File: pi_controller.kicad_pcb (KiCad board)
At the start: 4 copper layers, 149 parts, among them J1 DC Supply, J10 CS5, J11 CS7, J12 ROW1, J13 ROW2, J14 ROW3, J15 LED1, J16 LED2, J17 LED3, J18 LED4, J19 ROW4, J2 I2C, J20 ROW5, J21 ROW6, J22 LED5, J23 LED6, J24 LED7, J25 LED8, J26 ROW7, J27 ROW8, J28 AN1, J29 AN3, J3 UART, J30 AN5, J31 AN7, J32 AN9, J33 AN11, J34 AN13, J35 AN15, J36 AN2, J37 AN4, J38 AN6, J39 AN8, J4 PWM, J40 AN10, J41 AN12, J42 AN14, J43 AN16, J5 CS2, J6 CS4, J7 CS6, J8 CS8, J9 CS3, Q1 AOD4184A, U1 AP62300TWU, U2 RaspberryPi_Pico, U3 LM4040DBZ-3, U4 74HC138, U5 74HC138, U6 TM1639 (TA2009B), U7 CD74HC4067SM96

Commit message: Update routing
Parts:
- added H1: MountingHole_Pad, MountingHole:MountingHole_2.2mm_M2_ISO14580_Pad_TopBottom, F.Cu at (196.0, 144.8)
- added H2: MountingHole_Pad, MountingHole:MountingHole_2.2mm_M2_ISO14580_Pad_TopBottom, F.Cu at (120.5, 61.2)
- added H3: MountingHole_Pad, MountingHole:MountingHole_2.2mm_M2_ISO14580_Pad_TopBottom, F.Cu at (196.1, 61.1)
- added H4: MountingHole_Pad, MountingHole:MountingHole_2.2mm_M2_ISO14580_Pad_TopBottom, F.Cu at (88.0, 145.0)
- moved J40 97.9 mm to (128.3, 70.9), turned to 180 degrees
- moved R2 96.5 mm to (149.9, 100.1)
- moved J41 96.5 mm to (136.1, 71.0), turned to 180 degrees
- moved R1 93.4 mm to (146.3, 100.1), turned to 180 degrees
- moved J2 93.4 mm to (151.5, 102.9), turned to -90 degrees
- moved J38 84.0 mm to (132.2, 78.9)
- moved J3 82.1 mm to (144.1, 110.2), turned to 90 degrees
- moved J37 80.7 mm to (140.1, 78.9)
- moved J32 77.7 mm to (124.3, 70.9), turned to 180 degrees
- moved J42 77.2 mm to (144.0, 71.0), turned to 180 degrees
- moved J30 76.9 mm to (136.1, 78.9)
- moved J33 76.8 mm to (132.2, 71.0), turned to 180 degrees
- moved J43 70.1 mm to (151.9, 70.9), turned to 180 degrees
- moved J39 69.5 mm to (124.3, 78.9)
- moved J34 68.4 mm to (140.1, 71.0), turned to 180 degrees
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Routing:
- net /COL_MUX_C: track 0.00 -> 169.2 mm, vias 0 -> 1
- net /COL_MUX_A: track 0.00 -> 167.8 mm, vias 0 -> 1
- net /COL_MUX_B: track 0.00 -> 153.4 mm, vias 0 -> 1
- net /MOSI: track 0.00 -> 125.6 mm, vias 0 -> 2
- net /SCLK: track 0.00 -> 113.8 mm, vias 0 -> 2
- net VDDA: track 6.54 -> 119.4 mm
- net /COL8: track 0.00 -> 107.0 mm
- net /COL1: track 0.00 -> 104.5 mm
- net /GRID1: track 0.00 -> 103.6 mm, vias 0 -> 1
- net /COL2: track 0.00 -> 103.2 mm
- net /COL3: track 0.00 -> 102.0 mm
- net /COL4: track 0.00 -> 101.5 mm
- net /COL5: track 0.00 -> 100.9 mm
- net /COL7: track 0.00 -> 100.5 mm
- net /COL6: track 0.00 -> 100.4 mm
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- added copper zone on In2.Cu, net +3V3
- added copper zone on In1.Cu, net GND
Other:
- board outline added: 114 x 88.8 mm

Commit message: Minor adjustments
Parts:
- moved J2 7.45 mm to (144.1, 101.7), turned to 90 degrees
- moved TP1 7.15 mm to (117.6, 105.8)
- moved TP4 6.22 mm to (110.9, 105.7)
- moved R2 6.07 mm to (145.8, 104.5), turned to 180 degrees
- moved R1 5.38 mm to (149.3, 104.5), turned to 0 degrees
- moved C7 0.13 mm to (102.6, 93.0)
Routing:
- net /SDA: track 2.80 -> 54.1 mm, vias 0 -> 1
- net /SCL: track 3.12 -> 53.7 mm, vias 0 -> 1
- net /SCLK: track 113.8 -> 121.3 mm
- net VDDA: track 119.4 -> 113.2 mm
- net /CS_KEY: track 79.3 -> 84.5 mm
- net /UART0_RX: track 21.3 -> 25.3 mm
- net /COL_MUX_B: track 153.4 -> 156.9 mm
- net +9V: track 0.00 -> 2.72 mm
- net GND: track 64.2 -> 66.6 mm, vias 22 -> 24
- net /PWM_OUT: track 22.8 -> 23.6 mm
- net /AN14: track 39.4 -> 38.8 mm
- net /AN16: track 43.4 -> 44.0 mm
- net /ADC_MUX_D: vias 1 -> 3

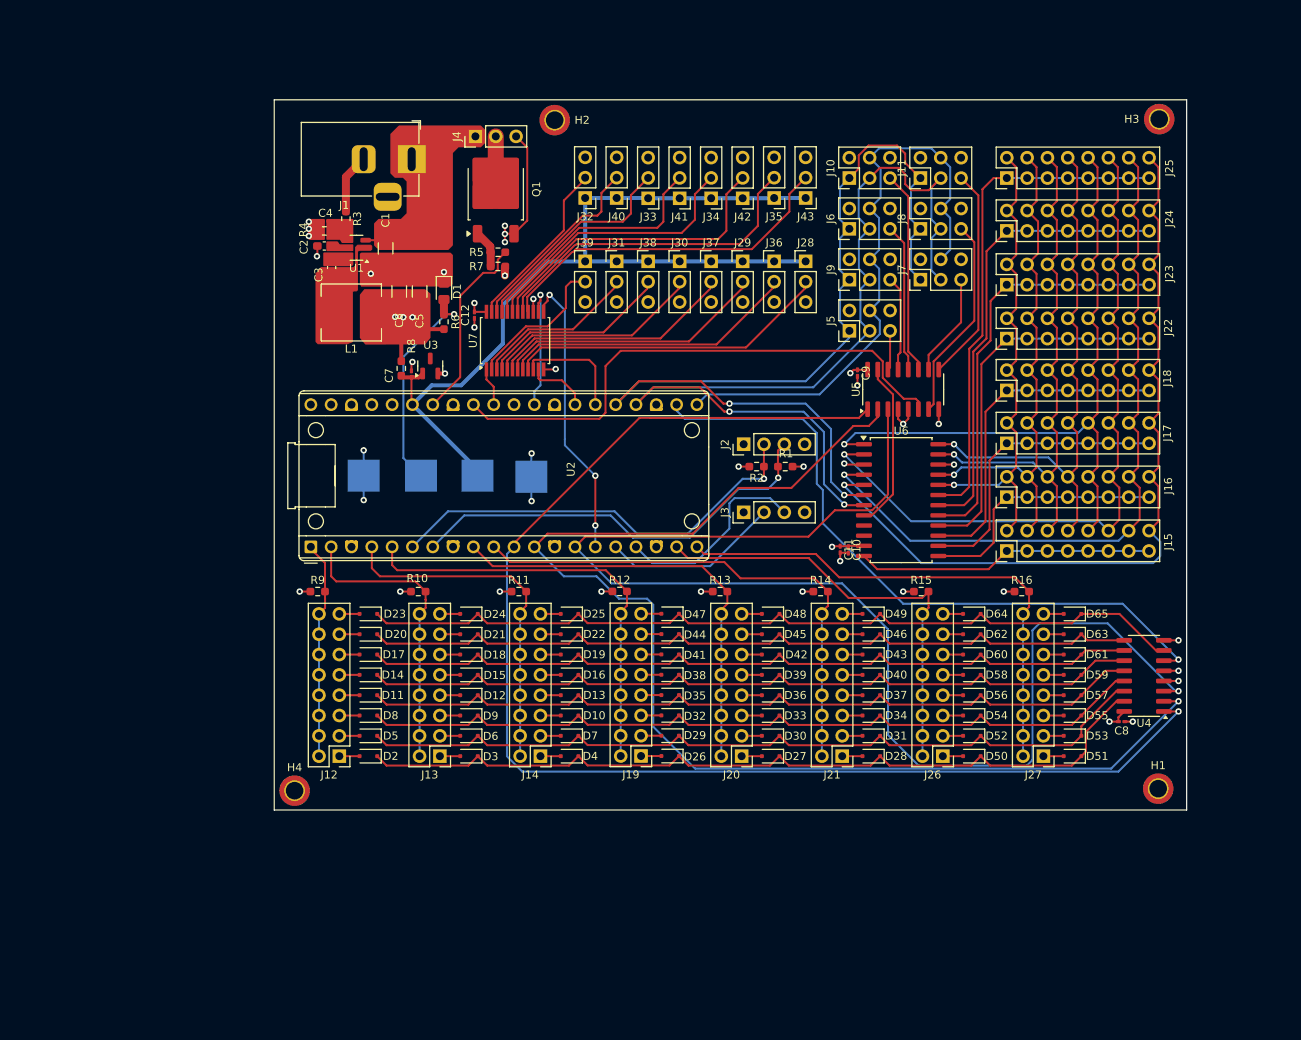
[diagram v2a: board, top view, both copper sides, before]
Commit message: Component repositioning to compact form factor
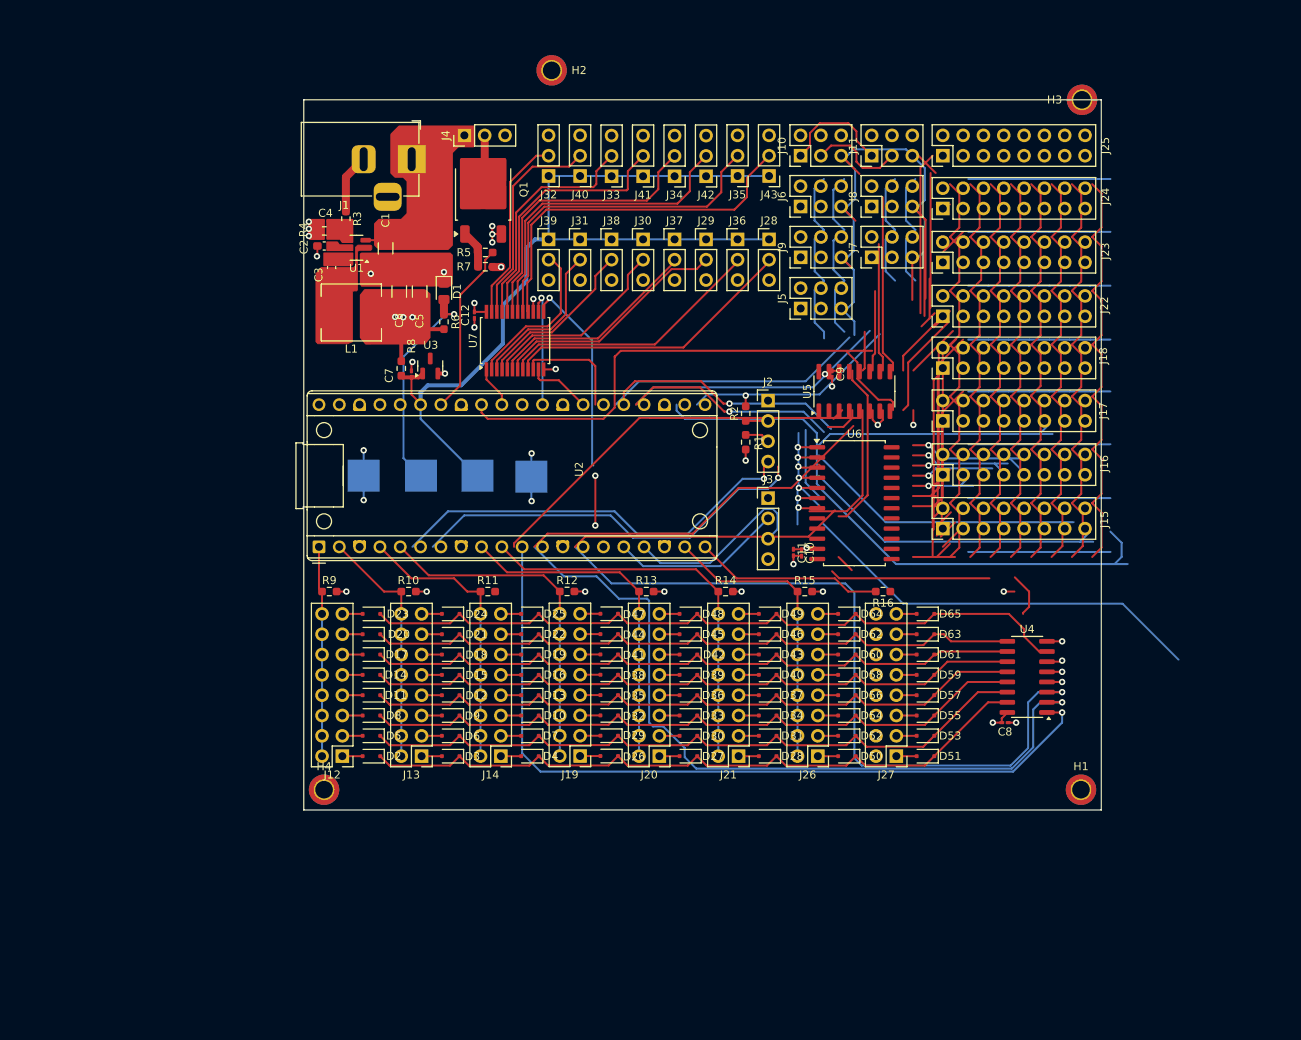
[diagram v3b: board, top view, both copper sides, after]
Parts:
- moved D51 18.4 mm to (166.9, 140.7)
- moved D53 18.4 mm to (166.9, 138.2)
- moved D55 18.4 mm to (166.9, 135.6)
- moved D57 18.4 mm to (166.9, 133.1)
- moved D59 18.4 mm to (166.9, 130.6)
- moved D61 18.4 mm to (166.9, 128.0)
- moved D63 18.4 mm to (166.9, 125.5)
- moved D65 18.4 mm to (166.9, 122.9)
- moved J27 18.4 mm to (163.2, 140.7)
- moved R16 17.3 mm to (161.6, 120.1), turned to 180 degrees
- moved D50 15.6 mm to (157.1, 140.7)
- moved D52 15.6 mm to (157.1, 138.2)
- moved D54 15.6 mm to (157.1, 135.6)
- moved D56 15.6 mm to (157.1, 133.1)
- moved D58 15.6 mm to (157.1, 130.6)
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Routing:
- net /ROW8: track 64.7 -> 23.7 mm
- net /COL_MUX_C: track 169.2 -> 145.8 mm
- net /SEG12: track 63.6 -> 41.3 mm
- net /CS1: track 21.1 -> 0.00 mm
- net /SEG9: track 46.8 -> 67.1 mm
- net /ROW7: track 55.4 -> 37.0 mm
- net GND: track 66.6 -> 84.7 mm, vias 24 -> 26
- net /GRID5: track 71.3 -> 53.4 mm, vias 1 -> 0
- net /COL1: track 104.5 -> 88.0 mm
- net /COL_MUX_A: track 167.8 -> 151.5 mm
- net /CS8: track 25.6 -> 41.4 mm
- net /COL2: track 103.2 -> 87.6 mm
- net /COL4: track 101.5 -> 86.4 mm
- net /COL5: track 100.9 -> 85.9 mm
- net /COL3: track 102.0 -> 86.9 mm
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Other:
- board size 114 x 88.8 mm -> 99.7 x 88.8 mm

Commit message: Adjusting DRC checks
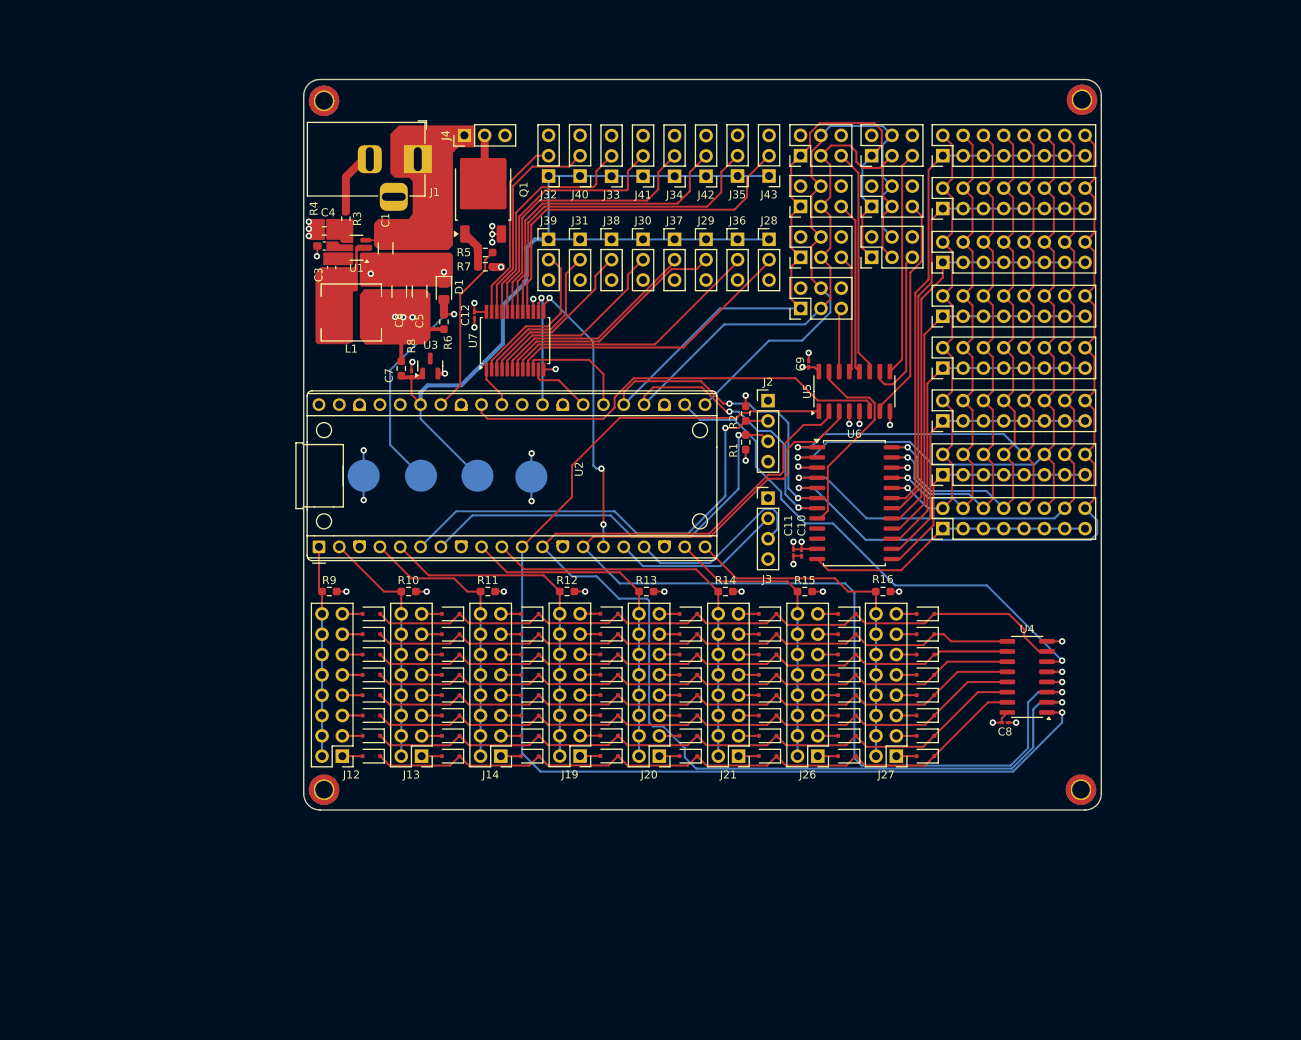
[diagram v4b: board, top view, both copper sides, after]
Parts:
- TP1, TP2, TP3, TP4: footprint TestPoint:TestPoint_Pad_4.0x4.0mm -> TestPoint:TestPoint_Pad_D4.0mm
- moved H2 28.7 mm to (91.7, 58.8)
- moved C9 3.18 mm to (152.3, 91.7), turned to 90 degrees
- moved J1 0.76 mm to (103.4, 66.1)
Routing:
- net GND: track 84.7 -> 51.2 mm, vias 26 -> 25
- net /CS1: track 0.00 -> 25.5 mm
- net /SEG12: track 41.3 -> 64.2 mm
- net /MISO: track 91.3 -> 70.5 mm
- net /ROW8: track 23.7 -> 44.2 mm
- net /SEG9: track 67.1 -> 47.6 mm
- net /GRID5: track 53.4 -> 72.2 mm, vias 0 -> 1
- net /CS_KEY: track 80.3 -> 64.7 mm
- net /CS5: track 13.3 -> 28.5 mm
- net /CS6: track 5.33 -> 19.8 mm
- net /SEG3: track 50.2 -> 37.0 mm, vias 1 -> 0
- net /CS8: track 41.4 -> 28.2 mm
- net /CS3: track 1.84 -> 14.9 mm
- net /CS_LED: track 68.0 -> 55.0 mm
- net /SCLK: track 121.3 -> 108.7 mm
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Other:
- board size 99.7 x 88.8 mm -> 99.7 x 91.3 mm
- board text added: "2.03 x 2.03 radius"

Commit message: Update PCB footprints
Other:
- board text added: "Analog Inputs 1- VDA 2- Wiper 3- Gnd"
- board text added: "SPI Interfaces"
- board text added: "UART"
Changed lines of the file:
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@@
 		(tags "resistor handsolder")
 		(property "Reference" "R1"
-			(at 1.016 1.524 90)
+			(at 0.635 1.397 90)
 			(layer "F.SilkS")
 			(effects
@@
 		)
 		(fp_line
-			(start 0.9 1.9)
+			(start 0.9 2)
 			(end 0.9 4.6)
 			(stroke
@@
 		(tags "resistor handsolder")
 		(property "Reference" "R2"
-			(at -1.0395 -1.524 90)
+			(at -1.0395 -1.397 90)
 			(layer "F.SilkS")
 			(effects
@@
 		(attr through_hole)
 		(fp_line
-			(start 4.11 -27.01)
-			(end 4.11 -26.09)
+			(start 10 -25.61)
+			(end 7.51 -25.61)
 			(stroke
 				(width 0.12)
@@
 		)
 		(fp_line
-			(start -4.11 -27.01)
-			(end 4.11 -27.01)
+			(start 7.51 -25.61)
+			(end 7.51 -24.69648)
 			(stroke
 				(width 0.12)
@@
 		)
 		(fp_line
-			(start -4.11 -27.01)
-			(end -4.11 -26.09)
+			(start 4.17 -25.61)
+			(end 7.51 -25.61)
 			(stroke
 				(width 0.12)
@@
 		)
 		(fp_line
-			(start 4.11 -26.09)
-			(end 3.9 -26.09)
+			(start -3.97 -25.61)
+			(end 4.28 -25.61)
 			(stroke
 				(width 0.12)
@@
 		)
 		(fp_line
-			(start 3.9 -26.09)
-			(end 3.9 -24.694)
+			(start -7.51 -25.61)
+			(end -3.97 -25.61)
 			(stroke
 				(width 0.12)
@@
 		)
 		(fp_line
-			(start -3.9 -26.09)
-			(end -3.9 -24.694)
+			(start -7.51 -25.61)
+			(end -7.51 -24.69648)
 			(stroke
 				(width 0.12)
@@
 		)
 		(fp_line
-			(start -4.11 -26.09)
-			(end -3.9 -26.09)
+			(start -10 -25.61)
+			(end -7.51 -25.61)
 			(stroke
 				(width 0.12)
@@
 		)
 		(fp_line
-			(start 10 -25.61)
-			(end 7.51 -25.61)
+			(start 4.11 -25.6032)
+			(end 4.11 -24.6832)
 			(stroke
 				(width 0.12)
@@
 		)
 		(fp_line
-			(start 7.51 -25.61)
-			(end 7.51 -24.69648)
+			(start -4.11 -25.6032)
+			(end -4.11 -24.6832)
 			(stroke
 				(width 0.12)
@@
 		)
 		(fp_line
-			(start 4.235 -25.61)
-			(end 7.51 -25.61)
+			(start -10.27 -25.547)
+			(end -10.27 25.547)
 			(stroke
 				(width 0.12)
@@
 		)
 		(fp_line
-			(start -4.235 -25.61)
-			(end 4.235 -25.61)
+			(start 10.61 -25)
+			(end 10.61 25)
 			(stroke
 				(width 0.12)
@@
 		)
 		(fp_line
-			(start -7.51 -25.61)
-			(end -4.235 -25.61)
+			(start -10.61 -25)
+			(end -10.61 25)
 			(stroke
 				(width 0.12)
@@
 		)
 		(fp_line
-			(start -7.51 -25.61)
-			(end -7.51 -24.69648)
+			(start 7.51 -24.69648)
+			(end 7.51 -22.30352)
 			(stroke
 				(width 0.12)
@@
 		)
 		(fp_line
-			(start -10 -25.61)
-			(end -7.51 -25.61)
+			(start -7.51 -24.69648)
+			(end -7.51 -22.30352)
 			(stroke
 				(width 0.12)
@@
 		)
 		(fp_line
-			(start -10.27 -25.547)
-			(end -10.27 25.547)
+			(start 3.9 -24.694)
+			(end 3.9 -22.306)
 			(stroke
 				(width 0.12)
-				(type solid)
+				(type default)
 			)
 			(layer "F.SilkS")
 		)
 		(fp_line
-			(start 10.61 -25)
-			(end 10.61 25)
+			(start -3.9 -24.694)
+			(end -3.9 -22.306)
 			(stroke
 				(width 0.12)
-				(type solid)
+				(type default)
 			)
 			(layer "F.SilkS")
 		)
 		(fp_line
-			(start -10.61 -25)
-			(end -10.61 25)
+			(start 4.11 -24.6832)
+			(end 3.9 -24.6832)
 			(stroke
 				(width 0.12)
@@
 		)
 		(fp_line
-			(start 7.51 -24.69648)
-			(end 7.51 -22.30352)
+			(start 3.9 -24.6832)
+			(end 3.9 -23.2872)
 			(stroke
 				(width 0.12)
@@
 		)
 		(fp_line
-			(start -7.51 -24.69648)
-			(end -7.51 -22.30352)
+			(start -3.9 -24.6832)
+			(end -3.9 -23.2872)
 			(stroke
 				(width 0.12)
@@
 		)
 		(fp_line
-			(start 3.9 -24.694)
-			(end 3.9 -22.306)
+			(start -4.11 -24.6832)
+			(end -3.9 -24.6832)
 			(stroke
 				(width 0.12)
-				(type default)
-			)
-			(layer "F.SilkS")
-		)
-		(fp_line
-			(start -3.9 -24.694)
-			(end -3.9 -22.306)
-			(stroke
-				(width 0.12)
-				(type default)
+				(type solid)
 			)
 			(layer "F.SilkS")
@@
 		(fp_poly
 			(pts
-				(xy 3.79 -21.2) (xy 3.79 -26.2) (xy 4 -26.2) (xy 4 -26.9) (xy -4 -26.9) (xy -4 -26.2) (xy -3.79 -26.2)
-				(xy -3.79 -21.2)
+				(xy 3.79 -21.2) (xy 3.79 -24.7904) (xy 4.0132 -24.7904) (xy 4.0132 -25.3492) (xy -4.0132 -25.3492)
+				(xy -4.0132 -24.7904) (xy -3.79 -24.7904) (xy -3.79 -21.2)
 			)
 			(stroke
@@
 		)
 		(fp_text user "${REFERENCE}"
-			(at 0 0 360)
+			(at 0.084 24.401 -90)
 			(layer "F.Fab")
 			(effects
@@
 		)
 		(group ""
-			(members "2646626f-3226-476e-bf4c-3d579709c044" "3704ffaa-dbbb-4da7-858c-14cb0424dd8d"
-				"4ba47d3a-43f8-4097-bc15-458fb810d474" "687c525b-7fe1-4e01-9ef9-63893dd76d1e"
-				"738a19d3-20ee-454a-ada1-3f4b2cac0b83" "93851b35-f911-4533-b25b-d64fbfd2a055"
-				"b19894cc-233f-4fca-b0ad-4d6b157d2181" "e088057c-4a2a-4883-b166-cee210829a6f"
-			)
-		)
-		(group ""
-			(members "5be00809-793c-4575-88c9-af6c156cc3e3" "5dc808f1-1ad2-4d82-b53a-339be024c766"
-				"61b49ba1-e006-429b-9a0e-e9dea97ee073" "646aa24a-b73b-41c0-a789-7f6e55234bf8"
-				"7884036b-77c5-4ebb-b68a-e1c50022c9ea" "849cfad4-072e-4d0f-a78f-95159eca27bb"
-				"8f0c9811-345c-4f6f-80b3-119b2904208e" "9b58e8fa-1eed-499b-aafd-84898567d050"
-				"c4036112-574f-486a-a8de-72c6bea74aa9" "dfe2bc5d-9716-4555-8132-bbd50e759a71"
-				"e701a5ba-01e5-430d-a5b0-014c02f8d0aa" "eff28fdf-8093-467d-81fe-f5fe5485abcd"
-			)
-		)
-		(group ""
 			(members "6207e867-1a35-47a8-8ce9-ad636b722732" "65c75b9c-4f2d-401d-853f-fac93e4d7d40")
 		)
@@
 				"4c075adb-7bfb-4d79-b53a-99b1b90aa57b" "563b85e2-65d0-46b2-b2c9-adc0f08d7a8c"
 				"81f87357-9f09-4fd2-8eca-16dfedbfb7df" "8af63139-80e0-4d1f-835c-ff931e5a9630"
-				"c5128fa3-bcb7-4315-bd03-ec95c603f6d8" "c7623e52-15f2-4cd6-acee-7c920f71d378"
-				"d2afa5d6-e4b2-47e9-abf4-1ff90d90d2ff" "d7d20f5e-8ea0-4fb9-a0c3-7fedcb7f0ddb"
-				"d82fe402-44ed-48ec-ae53-c13e327d779e"
+				"c5128fa3-bcb7-4315-bd03-ec95c603f6d8" "d2afa5d6-e4b2-47e9-abf4-1ff90d90d2ff"
+				"d7d20f5e-8ea0-4fb9-a0c3-7fedcb7f0ddb" "d82fe402-44ed-48ec-ae53-c13e327d779e"
 			)
 		)
@@
 		(layer "Edge.Cuts")
 	)
+	(gr_text "SPI Interfaces"
+		(at 149.86 88.392 0)
+		(layer "F.SilkS")
+		(effects
+			(font
+				(size 1 1)
+				(thickness 0.15)
+			)
+			(justify left bottom)
+		)
+	)
+	(gr_text "UART"
+		(at 145.288 115.316 90)
+		(layer "F.SilkS")
+		(effects
+			(font
+				(size 1 1)
+				(thickness 0.15)
+			)
+			(justify left bottom)
+		)
+	)
+	(gr_text "Analog Inputs\n1- VDA\n2- Wiper\n3- Gnd"
+		(at 122.428 90.17 0)
+		(layer "F.SilkS")
+		(effects
+			(font
+				(size 1 1)
+				(thickness 0.15)
+			)
+			(justify left bottom)
+		)
+	)
 	(gr_text "2.03 x 2.03 radius"

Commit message: Created gerber for quote and updated layout
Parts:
- moved L1 0.35 mm to (95.4, 85.5)
- moved C6 0.24 mm to (92.8, 79.5)
- moved C4 0.20 mm to (99.2, 77.2)
- renumbered C12 to C1, C11 to C10, C10 to C11, C8 to C12, C5 to C2, C6 to C3, C1 to C4, C2 to C5, C3 to C6, C4 to C7, C7 to C8, D12 to D10, D5 to D12, D6 to D13, D9 to D14, D21 to D15, D47 to D16, D45 to D17, D44 to D18, D48 to D19, D8 to D2, D42 to D20, D41 to D21, D39 to D22, D38 to D23, D36 to D24, D35 to D25, D19 to D26, D33 to D27, D32 to D28, D22 to D29, D23 to D3, D29 to D31, D13 to D32, D10 to D33, D16 to D34, D25 to D35, D7 to D36, D62 to D37, D56 to D38, D58 to D39, D24 to D4, D31 to D40, D34 to D41, D37 to D42, D40 to D43, D43 to D44, D46 to D45, D49 to D46, D64 to D47, D52 to D48, D60 to D49, D20 to D5, D54 to D50, D59 to D51, D63 to D52, D61 to D53, D65 to D54, D57 to D55, D53 to D56, D55 to D57, D2 to D58, D3 to D59, D18 to D6, D4 to D60, D27 to D61, D26 to D62, D50 to D63, D28 to D64, D51 to D65, D17 to D7, D15 to D8, D14 to D9, H2 to H1, H3 to H2, H4 to H3, H1 to H4, J4 to J1, J37 to J10, J38 to J11, J39 to J12, J40 to J13, J42 to J14, J35 to J15, J36 to J16, J5 to J17, J6 to J18, J7 to J19, J1 to J2, J8 to J20, J9 to J21, J10 to J22, J11 to J23, J28 to J24, J43 to J25, J23 to J26, J22 to J27, J24 to J28, J25 to J29, J41 to J3, J2 to J30, J3 to J31, J17 to J32, J15 to J33, J16 to J34, J18 to J35, J12 to J36, J13 to J37, J14 to J38, J20 to J39, J31 to J4, J19 to J40, J21 to J41, J26 to J42, J27 to J43, J32 to J5, J33 to J6, J30 to J7, J29 to J8, J34 to J9, R3 to R1, R11 to R10, R10 to R11, R15 to R14, R16 to R15, R14 to R16, R4 to R2, R5 to R3, R6 to R4, R7 to R5, R8 to R6, R1 to R7, R2 to R8, TP4 to TP2, TP2 to TP4, U7 to U2, U2 to U4, U4 to U7
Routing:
- net GND: track 51.2 -> 36.4 mm, vias 25 -> 49
- net +3V3: track 44.4 -> 36.5 mm, vias 23 -> 25
- net +9V: track 2.72 -> 0.77 mm
- net /CS1: track 25.5 -> 26.9 mm
- net /CS_LED: track 55.0 -> 56.0 mm
- net /AN11: track 28.9 -> 29.6 mm
- net /AN12: track 32.5 -> 33.0 mm
- added copper zone on F.Cu, net +3V3
- added copper zone on F.Cu, net +9V
- added copper zone on F.Cu, net GND
- added copper zone on F.Cu, net Net-(U1-BST)
- added copper zone on F.Cu, net Net-(U1-EN)
- added copper zone on F.Cu, net Net-(U1-FB)
- added copper zone on F.Cu, net Net-(U1-SW)
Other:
- board text added: "Key / Encoder Matrix"
- board text added: "LED Matrix"
